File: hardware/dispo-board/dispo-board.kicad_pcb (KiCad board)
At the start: 4 copper layers, 84.3 x 56.4 mm, 104 parts, among them J1 Conn_01x03, J10 Conn_01x02, J11 Conn_01x02, J12 Conn_01x03, J13 Conn_01x03, J14 Conn_ARM_JTAG_SWD_10, J2 Conn_01x03, J3 Conn_01x03, J4 Conn_01x04, J5 USB_B_Micro, J6 Conn_01x02, J7 Conn_01x02, J8 Conn_01x02, J9 Conn_01x02, SW1 SW_Push, U1 TPS79633DCQ, U2 STM32H725RGV6, U3 OPA1671, U4 CS5343-CZZ, U5 OPA1671, U6 CS4344-CZZR, Y1 32M

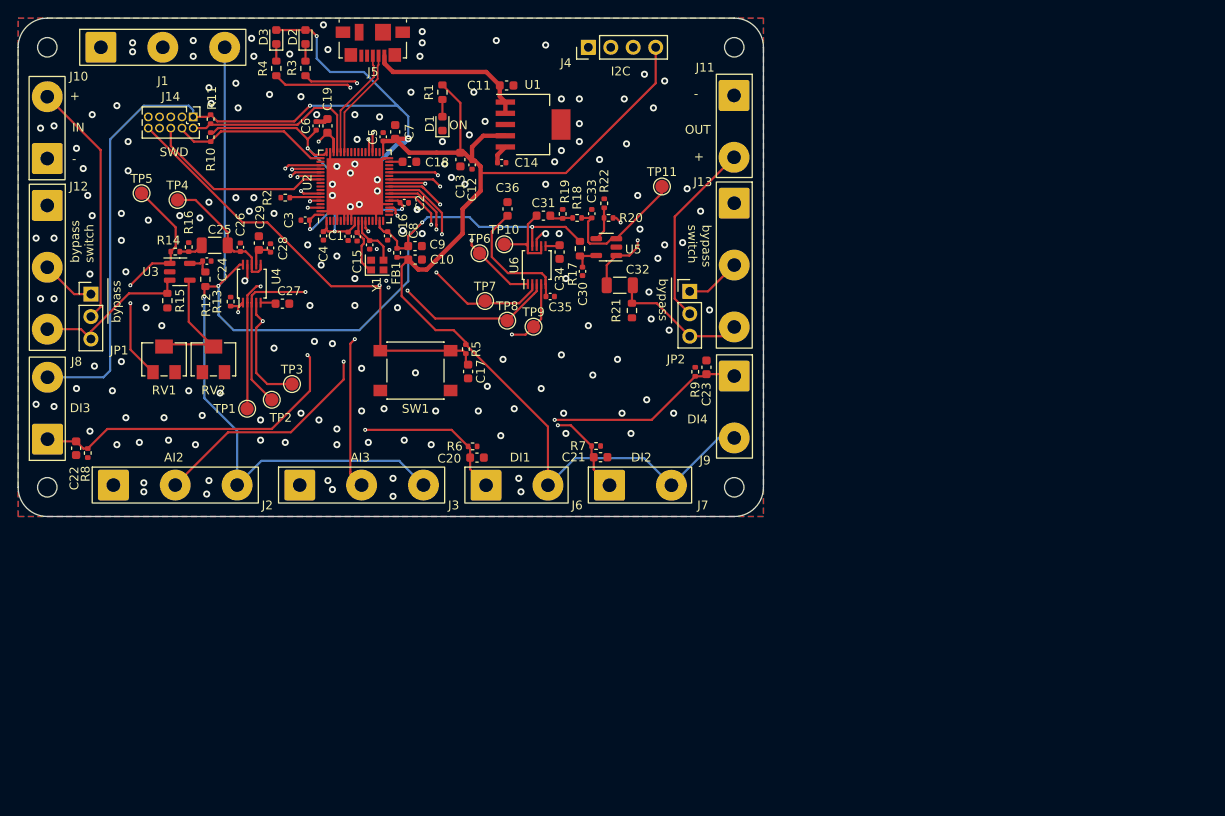
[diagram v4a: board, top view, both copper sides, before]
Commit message: changed to old ldo
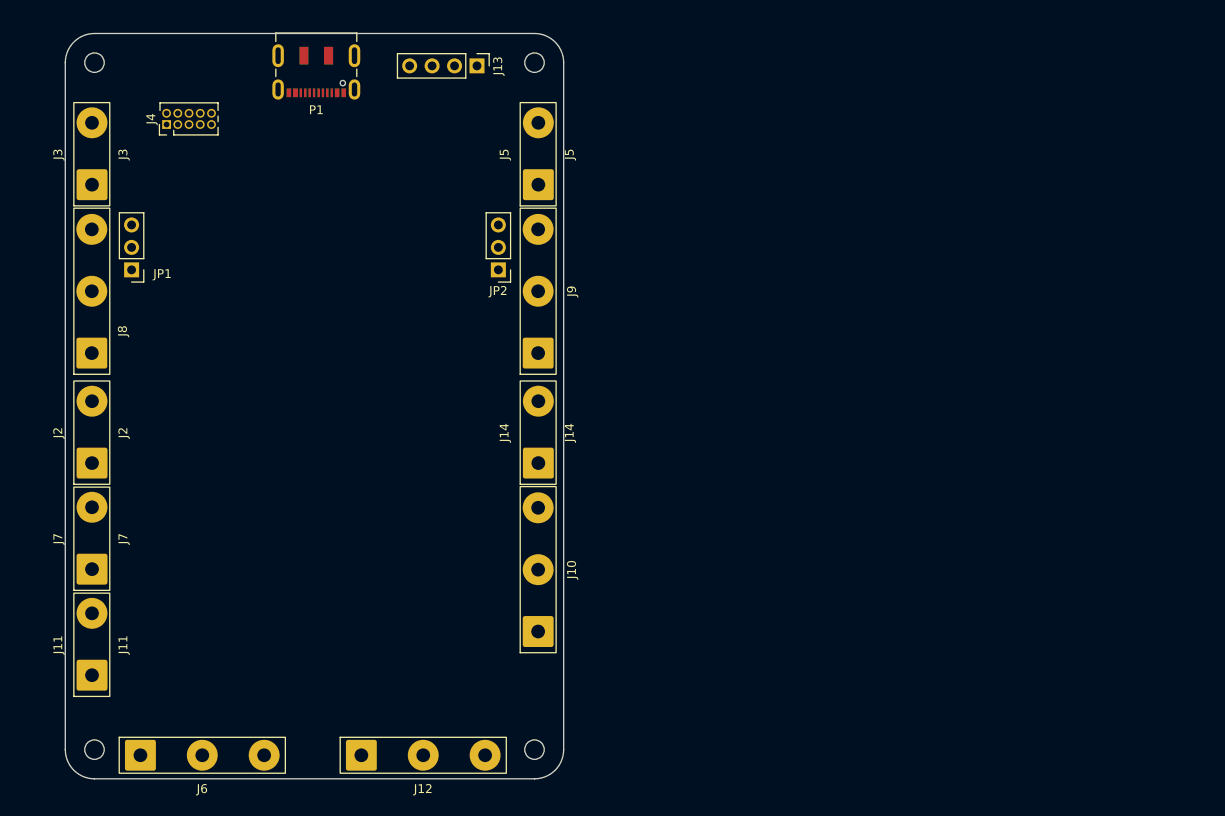
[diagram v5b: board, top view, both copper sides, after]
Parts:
- removed C1, C12, C2, C24, C3, C30, C4, C5, C6: 100n, Capacitor_SMD:C_0402_1005Metric
- removed C10, C13, C17, C20, C21, C22, C23, C9: 1u, Capacitor_SMD:C_0603_1608Metric
- removed C11, C18, C19: 2u2, Capacitor_SMD:C_0603_1608Metric
- removed C14, C33, C8: 10n, Capacitor_SMD:C_0402_1005Metric
- removed C15, C16: 16p, Capacitor_SMD:C_0402_1005Metric
- removed C25, C32: 1u, Capacitor_SMD:C_1206_3216Metric
- removed C26: 180p, Capacitor_SMD:C_0402_1005Metric
- removed C27, C29, C34, C36, C7: 10u, Capacitor_SMD:C_0603_1608Metric
- removed C28, C35: 0.1u, Capacitor_SMD:C_0402_1005Metric
- removed C31: 3u3, Capacitor_SMD:C_0603_1608Metric
- removed D1, D2, D3: LED power, LED_SMD:LED_0603_1608Metric
- removed FB1: 120R, Resistor_SMD:R_0402_1005Metric
- removed J1: Conn_01x03, MyFootprints:solder_pad_1x03_D3.5mm
- removed R1, R3, R4: 180, Resistor_SMD:R_0603_1608Metric
- removed R10, R11, R13, R16, R19, R2, R5, R6, R7, R8, R9: 10k, Resistor_SMD:R_0402_1005Metric
- removed R12, R17: 22, Resistor_SMD:R_0603_1608Metric
- removed R14: 1k, Resistor_SMD:R_0402_1005Metric
- removed R15, R21: 100k, Resistor_SMD:R_0603_1608Metric
- removed R18: 470, Resistor_SMD:R_0402_1005Metric
- removed R20: 0, Resistor_SMD:R_0402_1005Metric
- removed R22: DNP, Resistor_SMD:R_0402_1005Metric
- removed the REF** at (107.2, 25.4)
- removed the REF** at (29.5, 75.2)
- removed the REF** at (29.5, 25.4)
- removed the REF** at (107.2, 75.2)
- removed RV1, RV2: Potentiometer, Potentiometer_SMD:Potentiometer_Bourns_3224W_Vertical
- removed SW1: SW_Push, Button_Switch_SMD:SW_Push_1P1T_NO_6x6mm_H9.5mm
- removed TP1, TP10, TP11, TP2, TP3, TP4, TP5, TP6, TP7, TP8, TP9: TestPoint, TestPoint:TestPoint_Pad_D1.5mm
- removed U1: TPS79633DCQ, Package_TO_SOT_SMD:SOT-223-6
- removed U2: STM32H725RGV6, Package_DFN_QFN:QFN-68-1EP_8x8mm_P0.4mm_EP6.4x6.4mm
- removed U3, U5: OPA1671, Package_TO_SOT_SMD:SOT-23-5
- removed U4: CS5343-CZZ, Package_SO:TSSOP-10_3x3mm_P0.5mm
- removed U6: CS4344-CZZR, Package_SO:TSSOP-10_3x3mm_P0.5mm
- removed Y1: 32M, Crystal:Crystal_SMD_2016-4Pin_2.0x1.6mm
- added P1: USB_C_Plug_USB2.0, Connector_USB:USB_C_Receptacle_JAE_DX07S016JA1R1500, F.Cu at (59.9, 27.5)
- added REF**: MountingHole_2.2mm_M2, MountingHole:MountingHole_2.2mm_M2, F.Cu at (34.8, 104.9)
- added REF**: MountingHole_2.2mm_M2, MountingHole:MountingHole_2.2mm_M2, F.Cu at (84.6, 104.9)
- added REF**: MountingHole_2.2mm_M2, MountingHole:MountingHole_2.2mm_M2, F.Cu at (84.6, 27.1)
- added REF**: MountingHole_2.2mm_M2, MountingHole:MountingHole_2.2mm_M2, F.Cu at (34.8, 27.1)
- J10, J6, J8, J9: value Conn_01x02 -> Conn_01x03; footprint MyFootprints:solder_pad_1x02_D3.5mm -> MyFootprints:solder_pad_1x03_D3.5mm
- J13: value Conn_01x03 -> Conn_01x04; footprint MyFootprints:solder_pad_1x03_D3.5mm -> Connector_PinHeader_2.54mm:PinHeader_1x04_P2.54mm_Vertical
- J14: value Conn_ARM_JTAG_SWD_10 -> Conn_01x02; footprint Connector_PinHeader_1.27mm:PinHeader_2x05_P1.27mm_Vertical -> MyFootprints:solder_pad_1x02_D3.5mm
- J2, J3: value Conn_01x03 -> Conn_01x02; footprint MyFootprints:solder_pad_1x03_D3.5mm -> MyFootprints:solder_pad_1x02_D3.5mm
- J4: value Conn_01x04 -> Conn_ARM_JTAG_SWD_10; footprint Connector_PinHeader_2.54mm:PinHeader_1x04_P2.54mm_Vertical -> Connector_PinHeader_1.27mm:PinHeader_2x05_P1.27mm_Vertical
- J5: value USB_B_Micro -> Conn_01x02; footprint Connector_USB:USB_Micro-B_Molex_47346-0001 -> MyFootprints:solder_pad_1x02_D3.5mm
- moved J11 93.4 mm to (34.5, 93.0), turned to 90 degrees
- moved J10 74.7 mm to (85.0, 84.5)
- moved J12 69.7 mm to (72.0, 105.5), turned to 0 degrees
- moved J7 62.3 mm to (34.5, 81.0), turned to 90 degrees
- moved J14 52.9 mm to (85.0, 69.0), turned to 90 degrees
- moved J4 48.5 mm to (43.0, 34.1)
- moved J3 48.3 mm to (34.5, 37.5), turned to 90 degrees
- moved J6 46.9 mm to (47.0, 105.5)
- moved J13 36.8 mm to (78.1, 27.5)
- moved J9 25.8 mm to (85.0, 53.0), turned to 90 degrees
- moved J5 22.6 mm to (85.0, 37.5), turned to 90 degrees
- moved JP2 21.8 mm to (80.5, 50.6), turned to 180 degrees
- moved G*** 17.2 mm to (108.5, 21.5)
- moved J8 14.2 mm to (34.5, 53.0)
- moved J2 11.1 mm to (34.5, 69.0), turned to 90 degrees
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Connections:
- J10 pad 2: GUITAR_IN_P -> ADC1_INP5
- J11 pad 1: GND -> DIG_IN3
- J11 pad 2: GUITAR_OUT_P -> +3V3
- J12 pad 1: GUITAR_bypass -> GND
- J12 pad 2: GUITAR_IN_switch -> ADC1_INP8
- J12 pad 3: GUITAR_IN_µC -> +3.3VA
- J13 pad 1: GUITAR_bypass -> GND
- J13 pad 2: GUITAR_OUT_switch -> I2C1_SDA
- J13 pad 3: GUITAR_OUT_µC -> I2C1_SCL
- J14 pad 1: +3V3 -> DIG_IN4
- J14 pad 2: SWDIO -> +3V3
- J2 pad 1: GND -> DIG_IN1
- J2 pad 2: ADC1_INP5 -> +3V3
- J3 pad 2: ADC1_INP8 -> GUITAR_IN
- J4 pad 1: GND -> +3V3
- J4 pad 2: I2C1_SDA -> SWDIO
- J4 pad 3: I2C1_SCL -> GND
- J4 pad 4: +3V3 -> SWCLK
- J5 pad 1: 5V_IN -> GND
- J5 pad 2: USBD- -> GUITAR_OUT
- J6 pad 1: DIG_IN1 -> GND
- J6 pad 2: +3V3 -> ADC1_INP4
- J8 pad 1: DIG_IN3 -> GUITAR_bypass
- J8 pad 2: +3V3 -> GUITAR_IN_switch
- J9 pad 1: DIG_IN4 -> GUITAR_bypass
- J9 pad 2: +3V3 -> GUITAR_OUT_switch
- JP1 pad 2: GUITAR_IN_P -> GUITAR_IN
- JP2 pad 2: GUITAR_OUT_P -> GUITAR_OUT
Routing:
- net +3V3: track 287.9 -> 0.00 mm, vias 7 -> 0
- net +3.3VA: track 145.4 -> 0.00 mm, vias 4 -> 0
- net GUITAR_bypass: track 108.4 -> 0.00 mm
- net DIG_IN4: track 76.9 -> 0.00 mm, vias 2 -> 0
- net DIG_IN2: track 68.2 -> 0.00 mm, vias 2 -> 0
- net I2S6_MCK: track 67.9 -> 0.00 mm, vias 3 -> 0
- net I2S6_WS: track 64.2 -> 0.00 mm, vias 3 -> 0
- net I2S6_CK: track 63.4 -> 0.00 mm, vias 3 -> 0
- net ADC1_INP5: track 63.2 -> 0.00 mm, vias 2 -> 0
- net DIG_IN3: track 61.9 -> 0.00 mm, vias 2 -> 0
- net NRST: track 61.4 -> 0.00 mm, vias 2 -> 0
- net DIG_IN1: track 55.5 -> 0.00 mm, vias 2 -> 0
- net ADC1_INP8: track 50.3 -> 0.00 mm, vias 2 -> 0
- net GND: track 48.0 -> 0.00 mm, vias 171 -> 0
- net I2C1_SCL: track 47.2 -> 0.00 mm, vias 1 -> 0
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- removed copper zone on B.Cu, net GND
- removed copper zone on F.Cu, net GND
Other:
- board size 84.3 x 56.4 mm -> 56.4 x 84.3 mm
- copper layers 4 -> 2
- board text removed: "+"
- board text removed: "-"
- board text removed: "AI2"
- board text removed: "AI3"
- board text removed: "DI1"
- board text removed: "DI2"
- board text removed: "DI3"
- board text removed: "DI4"
- board text removed: "I2C"
- board text removed: "IN"
- board text removed: "ON"
- board text removed: "OUT"
- board text removed: "SWD"
- board text removed: "bypass"
- board text removed: "bypass switch"

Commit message: shorted board
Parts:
- removed the J12 at (72.0, 105.5)
- removed J14: Conn_01x02, MyFootprints:solder_pad_1x02_D3.5mm
- removed the J3 at (34.5, 37.5)
- added C1: 100n, Capacitor_SMD:C_0402_1005Metric, F.Cu at (65.1, 76.7)
- added C10: 100n, Capacitor_SMD:C_0402_1005Metric, F.Cu at (54.8, 72.6)
- added C11: 100n, Capacitor_SMD:C_0402_1005Metric, F.Cu at (54.8, 69.4)
- added C12: 100n, Capacitor_SMD:C_0402_1005Metric, F.Cu at (56.1, 67.9)
- added C13: 10u, Capacitor_SMD:C_0603_1608Metric, F.Cu at (55.6, 66.6)
- added C14: 16p, Capacitor_SMD:C_0402_1005Metric, F.Cu at (51.5, 75.2)
- added C15: 1u, Capacitor_SMD:C_0402_1005Metric, F.Cu at (159.0, 54.8)
- added C16: 16p, Capacitor_SMD:C_0402_1005Metric, F.Cu at (53.4, 77.4)
- added C17: 1u, Capacitor_SMD:C_0402_1005Metric, F.Cu at (132.5, 75.7)
- added C18: 1u, Capacitor_SMD:C_0402_1005Metric, F.Cu at (132.5, 77.6)
- added C19: 1u, Capacitor_SMD:C_0402_1005Metric, F.Cu at (132.5, 79.6)
- added C2: 1u, Capacitor_SMD:C_0402_1005Metric, F.Cu at (156.0, 48.6)
- added C20: 1u, Capacitor_SMD:C_0402_1005Metric, F.Cu at (132.5, 81.6)
- added C21: 100n, Capacitor_SMD:C_0402_1005Metric, F.Cu at (39.4, 64.5)
- added C22: 100n, Capacitor_SMD:C_0402_1005Metric, F.Cu at (74.3, 62.7)
- added C23: 10u, Capacitor_SMD:C_0603_1608Metric, F.Cu at (40.7, 64.8)
- added C24: 10u, Capacitor_SMD:C_0603_1608Metric, F.Cu at (73.0, 63.0)
- added C25: 10u, Capacitor_SMD:C_0603_1608Metric, F.Cu at (79.3, 59.9)
- added C26: 10u, Capacitor_SMD:C_0603_1608Metric, F.Cu at (46.7, 61.1)
- added C27: 180p, Capacitor_SMD:C_0402_1005Metric, F.Cu at (40.9, 62.3)
- added C28: 10n, Capacitor_SMD:C_0402_1005Metric, F.Cu at (77.5, 56.7)
- added C29: 100n, Capacitor_SMD:C_0402_1005Metric, F.Cu at (71.4, 55.3)
- added C3: 1u, Capacitor_SMD:C_0402_1005Metric, F.Cu at (156.0, 50.6)
- added C30: 100n, Capacitor_SMD:C_0402_1005Metric, F.Cu at (39.9, 59.8)
- added C31: 100n, Capacitor_SMD:C_1210_3225Metric, F.Cu at (76.2, 45.3)
- added C32: 100n, Capacitor_SMD:C_1210_3225Metric, F.Cu at (43.3, 45.4)
- added C33: 1u, Capacitor_SMD:C_0402_1005Metric, F.Cu at (56.8, 38.0)
- added C34: 10n, Capacitor_SMD:C_0402_1005Metric, F.Cu at (64.0, 46.0)
- added C35: 1u, Capacitor_SMD:C_0402_1005Metric, F.Cu at (55.8, 38.0)
- added C36: 1u, Capacitor_SMD:C_0402_1005Metric, F.Cu at (50.3, 35.8)
- added C37: 10n, Capacitor_SMD:C_0402_1005Metric, F.Cu at (59.1, 32.6)
- added C38: 1u, Capacitor_SMD:C_0402_1005Metric, F.Cu at (63.0, 46.0)
- added C39: 100n, Capacitor_SMD:C_0402_1005Metric, F.Cu at (54.8, 38.0)
- added C4: 100n, Capacitor_SMD:C_0402_1005Metric, F.Cu at (156.0, 52.6)
- added C40: 1u, Capacitor_SMD:C_0402_1005Metric, F.Cu at (59.1, 33.7)
- added C41: 10n, Capacitor_SMD:C_0402_1005Metric, F.Cu at (59.2, 42.7)
- added C42: 1u, Capacitor_SMD:C_0402_1005Metric, F.Cu at (50.2, 41.2)
- added C43: 1u, Capacitor_SMD:C_0402_1005Metric, F.Cu at (62.0, 46.0)
- added C44: 1u, Capacitor_SMD:C_0402_1005Metric, F.Cu at (56.8, 40.5)
- added C45: 100n, Capacitor_SMD:C_0402_1005Metric, F.Cu at (55.8, 40.5)
- added C5: 100n, Capacitor_SMD:C_0402_1005Metric, F.Cu at (156.0, 54.5)
- added C6: 100n, Capacitor_SMD:C_0402_1005Metric, F.Cu at (65.1, 69.4)
- added C7: 100n, Capacitor_SMD:C_0402_1005Metric, F.Cu at (158.9, 46.7)
- added C8: 100n, Capacitor_SMD:C_0402_1005Metric, F.Cu at (158.9, 48.6)
- added C9: 100n, Capacitor_SMD:C_0402_1005Metric, F.Cu at (58.3, 78.7)
- added D1: LED Status 1, LED_SMD:LED_0603_1608Metric, F.Cu at (159.5, 58.8)
- added D2: LED Status 2, LED_SMD:LED_0603_1608Metric, F.Cu at (159.5, 61.4)
- added D3: LED Power, LED_SMD:LED_0603_1608Metric, F.Cu at (54.5, 43.0)
- added FB1: 120R, Resistor_SMD:R_0402_1005Metric, F.Cu at (57.5, 33.1)
- added FB2: 120R, Resistor_SMD:R_0402_1005Metric, F.Cu at (62.5, 44.5)
- added J1: Conn_01x02, MyFootprints:solder_pad_1x02_D3.5mm, F.Cu at (34.5, 69.0)
- added J13: Conn_01x02, MyFootprints:solder_pad_1x02_D3.5mm, F.Cu at (85.0, 69.0)
- added J4: Conn_01x02, MyFootprints:solder_pad_1x02_D3.5mm, F.Cu at (85.0, 37.0)
- added R1: 10k, Resistor_SMD:R_0402_1005Metric, F.Cu at (156.0, 58.5)
- added R10: 10k, Resistor_SMD:R_0402_1005Metric, F.Cu at (129.6, 85.6)
- added R11: 10k, Resistor_SMD:R_0402_1005Metric, F.Cu at (140.7, 58.8)
- added R12: 10k, Resistor_SMD:R_0402_1005Metric, F.Cu at (80.6, 56.7)
- added R13: 10k, Resistor_SMD:R_0402_1005Metric, F.Cu at (79.6, 56.7)
- added R14: 470, Resistor_SMD:R_0402_1005Metric, F.Cu at (78.6, 56.7)
- added R15: 22, Resistor_SMD:R_0603_1608Metric, F.Cu at (72.7, 55.3)
- added R16: 22, Resistor_SMD:R_0603_1608Metric, F.Cu at (41.2, 59.7)
- added R17: 0, Resistor_SMD:R_0402_1005Metric, F.Cu at (77.5, 54.7)
- added R18: DNP, Resistor_SMD:R_0402_1005Metric, F.Cu at (143.6, 62.8)
- added R19: 100k, Resistor_SMD:R_0402_1005Metric, F.Cu at (146.5, 58.8)
- added R2: 220, Resistor_SMD:R_0402_1005Metric, F.Cu at (156.0, 60.5)
- added R20: 100k, Resistor_SMD:R_0402_1005Metric, F.Cu at (146.5, 60.8)
- added R21: 100k, Resistor_SMD:R_0402_1005Metric, F.Cu at (146.5, 62.8)
- added R22: 220, Resistor_SMD:R_0402_1005Metric, F.Cu at (54.8, 40.5)
- added R3: 10k, Resistor_SMD:R_0402_1005Metric, F.Cu at (156.0, 62.5)
- added R4: 220, Resistor_SMD:R_0402_1005Metric, F.Cu at (156.0, 64.5)
- added R5: 10k, Resistor_SMD:R_0402_1005Metric, F.Cu at (129.6, 75.7)
- added R6: 10k, Resistor_SMD:R_0402_1005Metric, F.Cu at (129.6, 77.7)
- added R7: 10k, Resistor_SMD:R_0402_1005Metric, F.Cu at (129.6, 79.7)
- added R8: 10k, Resistor_SMD:R_0402_1005Metric, F.Cu at (129.6, 81.7)
- added R9: 10k, Resistor_SMD:R_0402_1005Metric, F.Cu at (129.6, 83.6)
- added RST: SW_Push, Button_Switch_SMD:SW_Push_1P1T_NO_CK_KSC7xxJ, F.Cu at (69.4, 86.4)
- added RV1: Potentiometer, Potentiometer_SMD:Potentiometer_Bourns_3224W_Vertical, F.Cu at (45.3, 55.0)
- added RV2: Potentiometer, Potentiometer_SMD:Potentiometer_Bourns_3224W_Vertical, F.Cu at (39.9, 55.0)
- added TP1: TestPoint, TestPoint:TestPoint_Pad_D1.5mm, F.Cu at (129.9, 47.5)
- added TP10: TestPoint, TestPoint:TestPoint_Pad_D1.5mm, F.Cu at (133.5, 61.7)
- added TP2: TestPoint, TestPoint:TestPoint_Pad_D1.5mm, F.Cu at (129.9, 51.0)
- added TP3: TestPoint, TestPoint:TestPoint_Pad_D1.5mm, F.Cu at (129.9, 54.6)
- added TP4: TestPoint, TestPoint:TestPoint_Pad_D1.5mm, F.Cu at (129.9, 58.1)
- added TP5: TestPoint, TestPoint:TestPoint_Pad_D1.5mm, F.Cu at (129.9, 61.7)
- added TP6: TestPoint, TestPoint:TestPoint_Pad_D1.5mm, F.Cu at (133.5, 47.5)
- added TP7: TestPoint, TestPoint:TestPoint_Pad_D1.5mm, F.Cu at (133.5, 51.0)
- added TP8: TestPoint, TestPoint:TestPoint_Pad_D1.5mm, F.Cu at (133.5, 54.6)
- added TP9: TestPoint, TestPoint:TestPoint_Pad_D1.5mm, F.Cu at (133.5, 58.1)
- added U1: STM32H725RGVx, Package_DFN_QFN:QFN-68-1EP_8x8mm_P0.4mm_EP6.4x6.4mm, F.Cu at (60.0, 73.0)
- added U2: CS5343-CZZ, Package_SO:TSSOP-10_3x3mm_P0.5mm, F.Cu at (44.5, 64.5)
- added U3: CS4344, Package_SO:TSSOP-10_3x3mm_P0.5mm, F.Cu at (75.2, 59.6)
- added U4: OPA1671, Package_TO_SOT_SMD:SOT-23-5, F.Cu at (75.2, 55.6)
- added U5: OPA1671, Package_TO_SOT_SMD:SOT-23-5, F.Cu at (44.0, 60.2)
- added U6: TLV75710PDBV, Package_TO_SOT_SMD:SOT-23-5, F.Cu at (49.7, 38.5)
- added U7: TPS79633DCQ, Package_TO_SOT_SMD:SOT-223-6, F.Cu at (61.9, 38.5)
- added Y1: 32M, Crystal:Crystal_SMD_2016-4Pin_2.0x1.6mm, F.Cu at (53.3, 75.4)
- J10, J6: value Conn_01x03 -> Conn_01x02; footprint MyFootprints:solder_pad_1x03_D3.5mm -> MyFootprints:solder_pad_1x02_D3.5mm
- J11, J5, J7: value Conn_01x02 -> Conn_01x03; footprint MyFootprints:solder_pad_1x02_D3.5mm -> MyFootprints:solder_pad_1x03_D3.5mm
- moved J5 71.0 mm to (49.5, 99.0), turned to 0 degrees
- moved J10 70.0 mm to (45.5, 26.8), turned to 0 degrees
- moved J3 55.3 mm to (51.6, 88.8), turned to -90 degrees
- moved J8 50.5 mm to (85.0, 53.0)
- moved J11 36.0 mm to (70.0, 99.0), turned to 0 degrees
- moved J2 32.0 mm to (34.5, 37.0), turned to -90 degrees
- moved J9 32.0 mm to (85.0, 85.0)
- moved J7 28.0 mm to (34.5, 53.0)
- moved J6 27.1 mm to (34.5, 81.5), turned to 90 degrees
- moved REF** 6.50 mm to (34.8, 98.4)
- moved REF** 6.50 mm to (84.6, 98.4)
- renumbered J13 to J12, J4 to J3
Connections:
- J10 pad 1: GND -> DIG_IN3
- J10 pad 2: ADC1_INP5 -> +3V3
- J11 pad 1: DIG_IN3 -> GND
- J11 pad 2: +3V3 -> ADC1_INP8
- J2 pad 1: DIG_IN1 -> GND
- J2 pad 2: +3V3 -> GUITAR_IN
- J5 pad 2: GUITAR_OUT -> ADC1_INP4
- J6 pad 1: GND -> DIG_IN2
- J6 pad 2: ADC1_INP4 -> +3V3
- J7 pad 1: DIG_IN2 -> GUITAR_bypass
- J7 pad 2: +3V3 -> GUITAR_IN_switch
- J8 pad 2: GUITAR_IN_switch -> GUITAR_OUT_switch
- J8 pad 3: GUITAR_IN_µC -> GUITAR_OUT_µC
- J9 pad 1: GUITAR_bypass -> GND
- J9 pad 2: GUITAR_OUT_switch -> ADC1_INP5
- J9 pad 3: GUITAR_OUT_µC -> +3.3VA
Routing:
- net +3.3VA: track 0.00 -> 60.8 mm, vias 0 -> 8
- net Net-(U4-OUT): track 0.00 -> 16.4 mm
- net Net-(U2-AINL): track 0.00 -> 14.5 mm
- net GUITAR_IN: track 0.00 -> 14.3 mm
- net +3V3: track 0.00 -> 14.3 mm, vias 0 -> 2
- net GUITAR_OUT: track 0.00 -> 14.1 mm
- net +5V: track 0.00 -> 14.1 mm
- net Net-(U5--): track 0.00 -> 10.3 mm
- net Net-(C32-Pad1): track 0.00 -> 10.2 mm
- net Net-(U4-V+): track 0.00 -> 9.27 mm, vias 0 -> 2
- net 5V_USB: track 0.00 -> 8.05 mm
- net GUITAR_OUT_µC: track 0.00 -> 7.60 mm
- net GUITAR_IN_µC: track 0.00 -> 7.57 mm
- net Net-(U3-AOUTL): track 0.00 -> 6.72 mm
- net GUITAR_OUT_switch: track 0.00 -> 5.50 mm
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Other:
- board size 56.4 x 84.3 mm -> 56.4 x 77.8 mm
- copper layers 2 -> 4
- board text added: "dispo V0.2"
- board text removed: "dispo V1.0"

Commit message: routed i2s and analog and digital pins, rst button and debug connector not finished
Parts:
- moved D1 128.6 mm to (35.0, 90.9), turned to 180 degrees
- moved D2 128.4 mm to (35.0, 92.7), turned to 180 degrees
- moved R2 122.3 mm to (37.6, 90.9)
- moved R4 121.7 mm to (37.6, 92.7)
- moved C15 109.0 mm to (55.1, 87.8), turned to 90 degrees
- moved R3 105.0 mm to (54.1, 87.8), turned to -90 degrees
- moved R21 103.8 mm to (43.6, 49.4), turned to -90 degrees
- moved C18 102.9 mm to (40.7, 31.1), turned to 180 degrees
- moved R8 102.8 mm to (40.7, 30.1), turned to 180 degrees
- moved R20 102.6 mm to (44.6, 49.4), turned to 90 degrees
- moved C7 100.0 mm to (64.1, 78.7), turned to -90 degrees
- moved R1 97.6 mm to (58.8, 67.2), turned to 90 degrees
- moved C4 96.5 mm to (63.1, 78.7), turned to -90 degrees
- moved C2 95.7 mm to (65.1, 78.7), turned to -90 degrees
- moved C8 95.6 mm to (65.8, 70.7)
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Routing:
- net +3V3: track 14.3 -> 194.6 mm, vias 2 -> 6
- net +3.3VA: track 60.8 -> 161.8 mm, vias 8 -> 9
- net I2S6_MCK: track 0.00 -> 67.3 mm, vias 0 -> 3
- net I2S6_WS: track 0.00 -> 65.2 mm, vias 0 -> 3
- net I2S6_CK: track 0.00 -> 62.8 mm, vias 0 -> 3
- net +1V0: track 0.00 -> 59.6 mm, vias 0 -> 3
- net GUITAR_bypass: track 0.00 -> 53.0 mm
- net DIG_IN2: track 0.00 -> 52.8 mm, vias 0 -> 2
- net I2C1_SDA: track 0.00 -> 49.2 mm
- net I2C1_SCL: track 0.00 -> 47.9 mm
- net DIG_IN4: track 0.00 -> 44.8 mm, vias 0 -> 2
- net LED_STATUS2: track 0.00 -> 42.4 mm
- net LED_STATUS1: track 0.00 -> 40.4 mm
- net DIG_IN3: track 0.00 -> 36.8 mm, vias 0 -> 2
- net I2S6_SDO: track 0.00 -> 35.2 mm, vias 0 -> 2
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
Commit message: routing almost finished, need GND plane
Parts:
- moved TP9 94.7 mm to (38.9, 62.0)
- moved TP6 84.0 mm to (50.5, 60.4)
- moved TP2 80.8 mm to (50.5, 65.6)
- moved TP5 79.4 mm to (50.5, 63.0)
- moved TP7 65.7 mm to (69.1, 64.3)
- moved TP1 61.5 mm to (69.1, 56.5)
- moved TP3 61.0 mm to (69.1, 59.1)
- moved TP4 60.9 mm to (69.1, 61.7)
- moved TP10 54.5 mm to (79.6, 53.4)
- moved TP8 53.9 mm to (80.4, 63.7)
- moved G*** 38.2 mm to (73.4, 36.6)
- moved C25 3.35 mm to (76.8, 62.2), turned to 180 degrees
- moved C9 0.80 mm to (58.1, 79.6)
- moved C14 0.12 mm to (51.4, 75.2)
- moved C16 0.12 mm to (53.3, 77.4)
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- renumbered RST to SW1
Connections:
- TP2 pad 1: I2S6_CK -> I2S6_SDI
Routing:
- net +3V3: track 194.6 -> 301.1 mm, vias 6 -> 13
- net USBD-: track 0.00 -> 56.5 mm, vias 0 -> 2
- net USBD+: track 0.00 -> 53.6 mm, vias 0 -> 2
- net +3.3VA: track 161.8 -> 182.1 mm, vias 9 -> 10
- net NRST: track 33.3 -> 48.1 mm, vias 1 -> 3
- net Net-(U4-OUT): track 5.90 -> 14.6 mm
- net I2S6_MCK: track 67.3 -> 74.6 mm
- net Net-(U3-AOUTL): track 6.72 -> 13.3 mm
- net GUITAR_OUT_µC: track 5.68 -> 10.7 mm
- net I2S6_WS: track 65.2 -> 70.1 mm
- net GUITAR_IN_µC: track 4.91 -> 8.77 mm
- net Net-(U4-+): track 2.58 -> 5.83 mm
- net I2S6_SDO: track 35.2 -> 38.1 mm
- net Net-(U2-AINL): track 14.9 -> 17.3 mm
- net I2S6_SDI: track 30.6 -> 32.7 mm
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- added copper zone on B.Cu, net GND
- added copper zone on F.Cu, net GND
- added copper zone on In1.Cu, net GND
- added copper zone on In2.Cu, net GND
